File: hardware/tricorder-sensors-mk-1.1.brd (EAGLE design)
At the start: 22.9 x 22.9 mm, 21 parts, among them U1 VEML6075, U2 APDS-9250ALT, U3 SI1145QFN-EASIER, U4 TSL2591DFN6

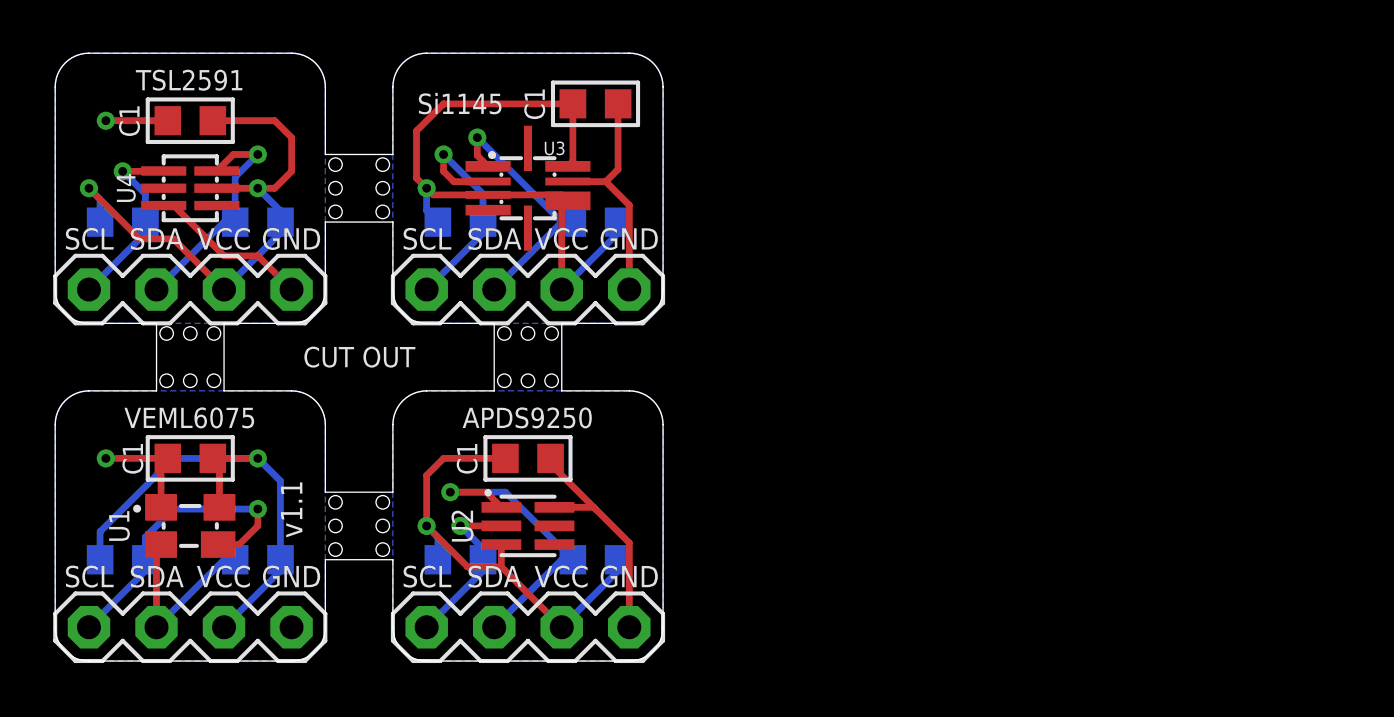
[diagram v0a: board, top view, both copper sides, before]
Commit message: relaid out, different set of sensors
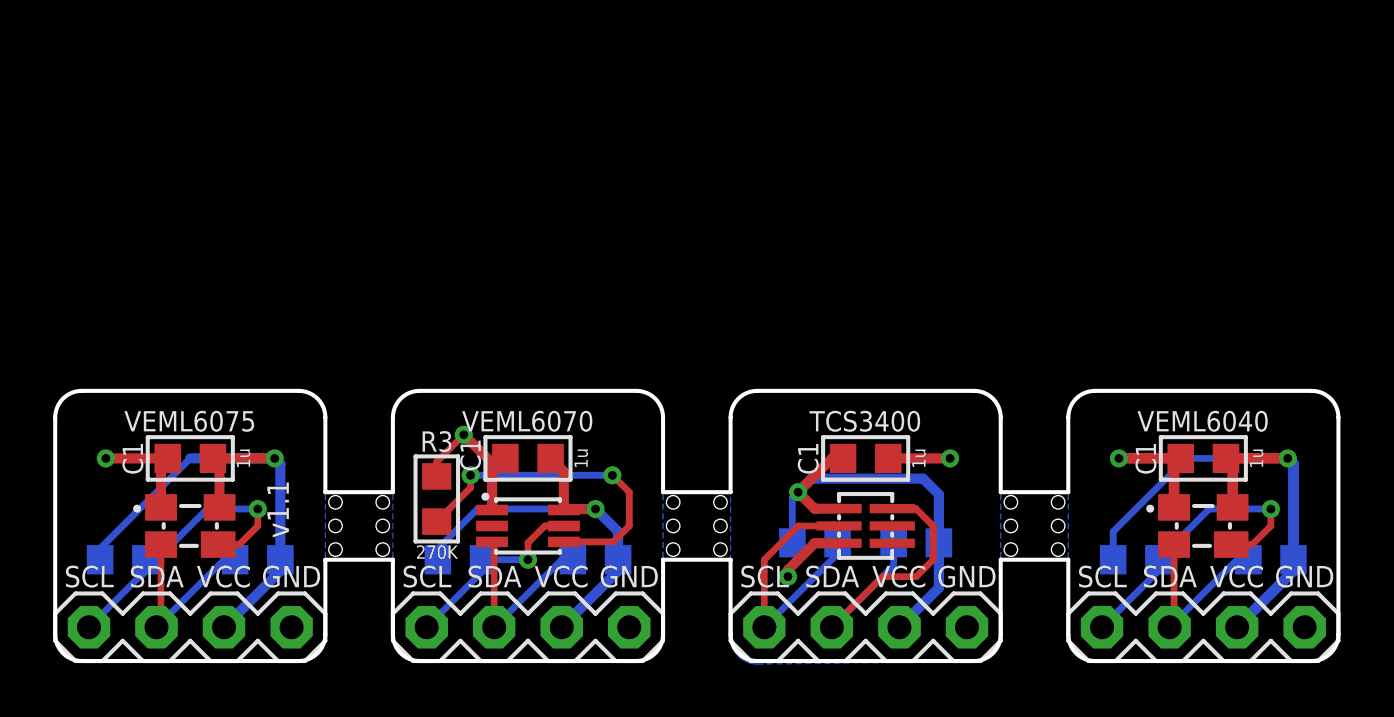
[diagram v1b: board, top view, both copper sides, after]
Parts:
- added R3_2: 270K, a_parts:R0603
- C1_1, C1_2, C1_3, C1_4: value 100n -> 1u
- R1_1, R1_2, R1_3, R1_4, R2_1, R2_2, R2_3, R2_4: value 10k -> 4K7
- U2: value APDS-9250ALT -> VEML6070; device a_parts:APDS-9250-ALT -> a_parts:OPLGA6
- U3: value SI1145QFN-EASIER -> TCS3400DFN6; device a_parts:SI1145-ALT -> a_parts:TCS3400_DFN6
- U4: value TSL2591DFN6 -> VEML6040; device a_parts:TSL2951_DFN6 -> a_parts:OPLGA4
- moved C1_4 40.2 mm to (43.2, 7.62)
- moved I2C_4 40.2 mm to (43.2, 1.27)
- moved R1_4 40.2 mm to (40.6, 3.81)
- moved R2_4 40.2 mm to (45.7, 3.81)
- moved U4 40.2 mm to (43.2, 5.08)
- moved R2_3 21.0 mm to (32.4, 4.45), turned to 0 degrees
- moved I2C_3 18.0 mm to (30.5, 1.27)
- moved U3 18.0 mm to (30.5, 5.08)
- moved C1_3 16.8 mm to (30.5, 7.62)
- moved R1_3 14.6 mm to (28.6, 4.45), turned to 180 degrees
- turned C1_2 to 180 degrees
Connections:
- removed net GND_5: C1_3.2, I2C_3.GND, U3.GND
- removed net SCL_5: I2C_3.SCL, R2_3.2, U3.SCL
- removed net SDA_5: I2C_3.SDA, R1_3.2, U3.SDA
- removed net VDD_5: C1_3.1, I2C_3.VCC, R1_3.1, R2_3.1, U3.LED, U3.VCC@1, U3.VCC@2
- new net GND_3: C1_3.2, I2C_3.GND, U3.3
- new net N$1: R3_2.1, U2.4
- new net SCL_3: I2C_3.SCL, R1_3.2, U3.2
- new net SDA_3: I2C_3.SDA, R2_3.2, U3.6
- new net VDD_3: C1_3.1, I2C_3.VCC, R1_3.1, R2_3.1, U3.1
- net GND_2: now also R3_2.2, U2.1; no longer U2.6
- net GND_4: now also U4.1; no longer U4.3
- net SCL_2: now also U2.5; no longer U2.2
- net SCL_4: now also U4.3; no longer U4.1
- net SDA_2: now also U2.3; no longer U2.1
- net SDA_4: now also U4.2; no longer U4.6
- net VDD_2: now also U2.6; no longer U2.3
- net VDD_4: now also U4.4; no longer U4.5
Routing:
- net VDD_5: track 24.8 -> 0.00 mm, vias 1 -> 0
- net VDD_3: track 0.00 -> 17.4 mm, vias 0 -> 1
- net N$1: track 0.00 -> 12.6 mm, vias 0 -> 2
- net SDA_3: track 0.00 -> 12.1 mm
- net SCL_3: track 0.00 -> 10.2 mm
- net SDA_5: track 9.75 -> 0.00 mm, vias 1 -> 0
- net SCL_5: track 9.04 -> 0.00 mm, vias 1 -> 0
- net GND_5: track 8.97 -> 0.00 mm
- net GND_3: track 0.00 -> 4.91 mm, vias 0 -> 2
- net SDA_2: track 11.8 -> 7.26 mm, vias 1 -> 0
- net GND_4: track 8.44 -> 4.27 mm
- net SCL_4: track 7.22 -> 10.9 mm
- net GND_2: track 9.05 -> 5.96 mm, vias 0 -> 1
- net SDA_4: track 8.70 -> 7.19 mm, vias 1 -> 0
- net VDD_2: track 17.5 -> 16.0 mm
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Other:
- board size 22.9 x 22.9 mm -> 48.3 x 10.2 mm
- board text added: "R3"
- board text added: "TCS3400"
- board text added: "Tricorder TCS3400 RGBW+IR"
- board text added: "Tricorder VEML6040 RGBW"
- board text added: "Tricorder VEML6070 UVA"
- board text added: "VEML6040"
- board text added: "VEML6070"
- board text removed: "APDS9250"
- board text removed: "CUT OUT"
- board text removed: "Si1145"
- board text removed: "TSL2591"
- board text removed: "Tricorder APDS9250 RGB+ALS+IR"
- board text removed: "Tricorder Si1145 ALS, IR, UV"
- board text removed: "Tricorder TSL2591 ALS+IR"
